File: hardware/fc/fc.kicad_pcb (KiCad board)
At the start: 6 copper layers, 35 x 35 mm, 100 parts, among them J1 USB4110-GF-A, J2 Micro_SD_Card_Det1, J3 FROM_ESC, J4 CAM, J5 CAM_CC, J6 ELRS, J7 VTX, SW1 Push, U1 TPS7A8101DRBR, U10 TPS2116DRL, U11 OPA354AIDBVR, U12 RP2354A, U2 TPS7A8101DRBR, U3 LMR51420YFDDCR, U4 USBLC6-2SC6, U5 EMIF06-MSD02N16, U6 LSM6DSK320X, U8 TS5A3159ADCK, U9 TLV7031DCKR, X1 ABM8-272-T3

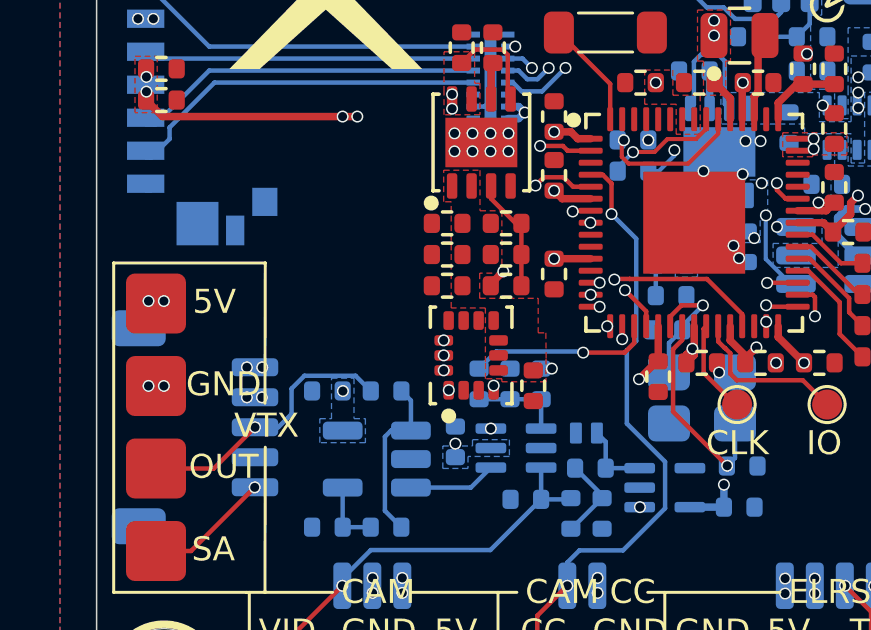
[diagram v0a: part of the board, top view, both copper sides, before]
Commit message: fc: route osd_en on l3
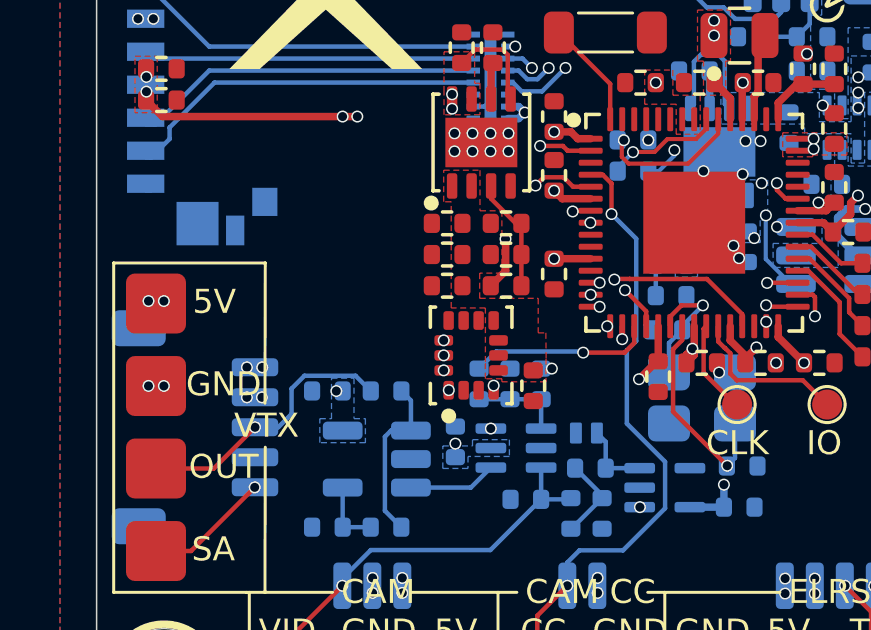
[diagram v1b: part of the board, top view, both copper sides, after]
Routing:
- net /OSD_EN: track 12.9 -> 16.6 mm
- net GND: track 6.22 -> 7.40 mm
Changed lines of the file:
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@@
 	)
 	(segment
+		(start 158.64 112.82)
+		(end 159.135 112.325)
+		(width 0.25)
+		(layer "F.Cu")
+		(net "GND")
+	)
+	(segment
 		(start 154.69 123.07)
 		(end 154.7 123.06)
@@
 	)
 	(segment
+		(start 159.135 112.325)
+		(end 159.135 111.265)
+		(width 0.25)
+		(layer "F.Cu")
+		(net "GND")
+	)
+	(segment
 		(start 167.629999 108)
 		(end 167.629999 107.998749)
@@
 	)
 	(segment
-		(start 158.640001 112.760328)
-		(end 159.056579 112.34375)
+		(start 159.135 111.265)
+		(end 159.13 111.26)
 		(width 0.25)
 		(layer "F.Cu")
@@
 	)
 	(via
-		(at 159.056579 112.34375)
-		(size 0.4)
-		(drill 0.3)
-		(layers "F.Cu" "B.Cu")
-		(net "GND")
-	)
-	(via
 		(at 162.58 126.41)
 		(size 0.4)
@@
 	)
 	(via
+		(at 159.13 111.26)
+		(size 0.4)
+		(drill 0.3)
+		(layers "F.Cu" "B.Cu")
+		(net "GND")
+	)
+	(via
 		(at 168.15 115.39)
 		(size 0.4)
@@
 	)
 	(via
-		(at 153.71 116.33)
-		(size 0.4)
-		(drill 0.3)
-		(layers "F.Cu" "B.Cu")
-		(net "V_3V3")
-	)
-	(via
 		(at 147.16 106.35)
 		(size 0.4)
@@
 	)
 	(via
+		(at 153.49 116.33)
+		(size 0.4)
+		(drill 0.3)
+		(layers "F.Cu" "B.Cu")
+		(net "V_3V3")
+	)
+	(via
 		(at 169.181044 105.090001)
 		(size 0.4)
@@
 	)
 	(segment
+		(start 153.702499 116.3275)
+		(end 153.4925 116.3275)
+		(width 0.25)
+		(layer "B.Cu")
+		(net "V_3V3")
+	)
+	(segment
 		(start 160.3175 115.582502)
 		(end 160.673812 115.582502)
@@
 	)
 	(segment
+		(start 153.4925 116.3275)
+		(end 153.49 116.33)
+		(width 0.25)
+		(layer "B.Cu")
+		(net "V_3V3")
+	)
+	(segment
 		(start 165.159999 112.110001)
 		(end 165.159999 112.22512)
@@
 	)
 	(segment
-		(start 160.130767 109.48025)
-		(end 160.130767 110.739233)
+		(start 150.965 119.54)
+		(end 150.77 119.54)
 		(width 0.15)
 		(layer "In2.Cu")
@@
 	)
 	(segment
-		(start 160.130767 110.739233)
-		(end 151.33 119.54)
+		(start 160.130767 110.789564)
+		(end 159.010331 111.91)
 		(width 0.15)
 		(layer "In2.Cu")
@@
 	)
 	(segment
-		(start 151.33 119.54)
-		(end 150.77 119.54)
+		(start 158.595 111.91)
+		(end 150.965 119.54)
+		(width 0.15)
+		(layer "In2.Cu")
+		(net "/VTX_SA")
+	)
+	(segment
+		(start 160.130767 109.48025)
+		(end 160.130767 110.789564)
+		(width 0.15)
+		(layer "In2.Cu")
+		(net "/VTX_SA")
+	)
+	(segment
+		(start 159.010331 111.91)
+		(end 158.595 111.91)
 		(width 0.15)
 		(layer "In2.Cu")
@@
 	)
 	(segment
-		(start 159.7 116.52)
-		(end 159.7 114.23)
+		(start 156.66 116.33)
+		(end 157.91 117.58)
 		(width 0.15)
-		(layer "In3.Cu")
+		(layer "In2.Cu")
 		(net "/OSD_EN")
 	)
 	(segment
-		(start 159.7 114.23)
-		(end 161.58625 112.34375)
+		(start 162.759015 112.613888)
+		(end 162.465127 112.32)
 		(width 0.15)
-		(layer "In3.Cu")
+		(layer "In2.Cu")
 		(net "/OSD_EN")
 	)
 	(segment
-		(start 158.64 117.58)
-		(end 159.7 116.52)
+		(start 158.79 112.32)
+		(end 156.66 114.45)
 		(width 0.15)
-		(layer "In3.Cu")
+		(layer "In2.Cu")
 		(net "/OSD_EN")
 	)
 	(segment
-		(start 161.58625 112.34375)
-		(end 162.488877 112.34375)
+		(start 162.465127 112.32)
+		(end 158.79 112.32)
 		(width 0.15)
-		(layer "In3.Cu")
+		(layer "In2.Cu")
 		(net "/OSD_EN")
 	)
 	(segment
-		(start 162.488877 112.34375)
-		(end 162.759015 112.613888)
+		(start 156.66 114.45)
+		(end 156.66 116.33)
 		(width 0.15)
-		(layer "In3.Cu")
+		(layer "In2.Cu")
+		(net "/OSD_EN")
+	)
+	(segment
+		(start 157.91 117.58)
+		(end 158.64 117.58)
+		(width 0.15)
+		(layer "In2.Cu")
 		(net "/OSD_EN")
 	)

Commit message: fc: clean up traces
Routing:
- net GND: track 7.40 -> 10.4 mm, vias 46 -> 48
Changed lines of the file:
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@@
 	)
 	(gr_circle
-		(center 147.749749 95.35)
-		(end 149.499749 95.35)
+		(center 147.749748 95.35)
+		(end 146.249748 95.35)
 		(stroke
-			(width 0.25)
-			(type dash)
+			(width 1)
+			(type solid)
 		)
 		(fill no)
@@
 	)
 	(gr_circle
-		(center 147.75 125.85)
-		(end 149.5 125.85)
+		(center 147.749748 125.85)
+		(end 146.249748 125.85)
 		(stroke
-			(width 0.25)
-			(type dash)
+			(width 1)
+			(type solid)
 		)
 		(fill no)
@@
 	)
 	(gr_circle
-		(center 178.25 95.35)
-		(end 180 95.35)
+		(center 178.249999 95.35)
+		(end 176.749999 95.35)
 		(stroke
-			(width 0.25)
-			(type dash)
+			(width 1)
+			(type solid)
 		)
 		(fill no)
@@
 	)
 	(gr_circle
-		(center 178.25 125.85)
-		(end 180 125.85)
+		(center 178.249999 125.85)
+		(end 176.749999 125.85)
 		(stroke
-			(width 0.25)
-			(type dash)
+			(width 1)
+			(type solid)
 		)
 		(fill no)
@@
 	)
 	(gr_circle
-		(center 147.749749 95.35)
-		(end 149.249749 95.35)
+		(center 147.749748 95.35)
+		(end 145.999748 95.35)
 		(stroke
-			(width 1)
-			(type solid)
+			(width 0.25)
+			(type dash)
 		)
 		(fill no)
@@
 	)
 	(gr_circle
-		(center 147.749749 125.85)
-		(end 149.249749 125.85)
+		(center 147.749748 125.85)
+		(end 145.999748 125.85)
 		(stroke
-			(width 1)
-			(type solid)
+			(width 0.25)
+			(type dash)
 		)
 		(fill no)
@@
 	)
 	(gr_circle
-		(center 178.25 95.35)
-		(end 179.75 95.35)
+		(center 178.249748 125.85)
+		(end 176.499748 125.85)
 		(stroke
-			(width 1)
-			(type solid)
+			(width 0.25)
+			(type dash)
 		)
 		(fill no)
@@
 	)
 	(gr_circle
-		(center 178.25 125.85)
-		(end 179.75 125.85)
+		(center 178.249999 95.35)
+		(end 176.499999 95.35)
 		(stroke
-			(width 1)
-			(type solid)
+			(width 0.25)
+			(type dash)
 		)
 		(fill no)
@@
 	)
 	(via
+		(at 158.623561 107.31875)
+		(size 0.4)
+		(drill 0.3)
+		(layers "F.Cu" "B.Cu")
+		(net "GND")
+	)
+	(via
 		(at 154.7 122.56)
 		(size 0.4)
@@
 	)
 	(via
+		(at 158.630166 104.319834)
+		(size 0.4)
+		(drill 0.3)
+		(layers "F.Cu" "B.Cu")
+		(net "GND")
+	)
+	(via
 		(at 167.631249 107.997499)
 		(size 0.4)
@@
 	)
 	(segment
+		(start 158.63 105.8475)
+		(end 158.63 107.312311)
+		(width 0.25)
+		(layer "B.Cu")
+		(net "GND")
+	)
+	(segment
+		(start 158.63 104.32)
+		(end 158.630166 104.319834)
+		(width 0.25)
+		(layer "B.Cu")
+		(net "GND")
+	)
+	(segment
+		(start 158.63 105.8475)
+		(end 158.63 104.32)
+		(width 0.25)
+		(layer "B.Cu")
+		(net "GND")
+	)
+	(segment
 		(start 171.12 110.26)
 		(end 170.490514 110.26)
@@
 	)
 	(segment
+		(start 158.63 107.312311)
+		(end 158.623561 107.31875)
+		(width 0.25)
+		(layer "B.Cu")
+		(net "GND")
+	)
+	(segment
 		(start 170.2 110.550514)
 		(end 170.2 111.169486)
@@
 	)
 	(segment
-		(start 158.774669 97.985)
+		(start 158.745 97.985)
 		(end 163.525 97.985)
 		(width 0.15)
@@
 	)
 	(segment
-		(start 158.545 98.214669)
-		(end 158.774669 97.985)
+		(start 160.284605 106.504605)
+		(end 158.24 104.46)
 		(width 0.15)
 		(layer "In2.Cu")
@@
 	)
 	(segment
-		(start 160.284605 106.504605)
-		(end 158.545 104.765)
+		(start 158.24 104.46)
+		(end 158.24 98.49)
 		(width 0.15)
 		(layer "In2.Cu")
@@
 	)
 	(segment
-		(start 163.525 97.985)
-		(end 163.91 98.37)
+		(start 160.284605 108.160001)
+		(end 160.284605 106.504605)
 		(width 0.15)
 		(layer "In2.Cu")
@@
 	)
 	(segment
-		(start 158.545 104.765)
-		(end 158.545 98.214669)
+		(start 163.525 97.985)
+		(end 163.91 98.37)
 		(width 0.15)
 		(layer "In2.Cu")
@@
 	)
 	(segment
-		(start 160.284605 108.160001)
-		(end 160.284605 106.504605)
+		(start 158.24 98.49)
+		(end 158.745 97.985)
 		(width 0.15)
 		(layer "In2.Cu")
@@
 	)
 	(segment
-		(start 163.487571 114.66276)
-		(end 163.175331 114.975)
+		(start 164.45 120.39)
+		(end 163.2 121.64)
 		(width 0.15)
 		(layer "B.Cu")
@@
 	)
 	(segment
-		(start 163.487571 111.252018)
-		(end 163.487571 114.66276)
+		(start 164.45 118.75)
+		(end 164.45 120.39)
 		(width 0.15)
 		(layer "B.Cu")
@@
 	)
 	(segment
-		(start 162.664807 110.429254)
-		(end 163.487571 111.252018)
+		(start 161.19 122.045001)
+		(end 161.19 122.82)
 		(width 0.15)
 		(layer "B.Cu")
@@
 	)
 	(segment
-		(start 163.175331 117.413299)
-		(end 164.45 118.687968)
+		(start 163.487571 111.252018)
+		(end 163.487571 115.087594)
 		(width 0.15)
 		(layer "B.Cu")
@@
 	)
 	(segment
-		(start 163.175331 114.975)
-		(end 163.175331 117.413299)
+		(start 163.487571 115.087594)
+		(end 163.175331 115.399834)
 		(width 0.15)
 		(layer "B.Cu")
@@
 	)
 	(segment
-		(start 164.45 118.687968)
-		(end 164.45 120.238656)
+		(start 163.2 121.64)
+		(end 161.595001 121.64)
 		(width 0.15)
 		(layer "B.Cu")
@@
 	)
 	(segment
-		(start 161.19 122.045001)
-		(end 161.19 122.82)
+		(start 163.175331 115.399834)
+		(end 163.175331 117.475331)
 		(width 0.15)
 		(layer "B.Cu")
@@
 	)
 	(segment
-		(start 163.048656 121.64)
-		(end 161.595001 121.64)
+		(start 162.664807 110.429254)
+		(end 163.487571 111.252018)
 		(width 0.15)
 		(layer "B.Cu")
@@
 	)
 	(segment
-		(start 164.45 120.238656)
-		(end 163.048656 121.64)
+		(start 163.175331 117.475331)
+		(end 164.45 118.75)
 		(width 0.15)
 		(layer "B.Cu")
@@
 	)
 	(segment
-		(start 163.205001 119.795001)
-		(end 163.61 120.2)
+		(start 163.205001 115.384999)
+		(end 163.205001 119.795001)
 		(width 0.15)
 		(layer "In2.Cu")
@@
 	)
 	(segment
-		(start 163.49 115.494138)
-		(end 163.205001 115.779137)
+		(start 163.49 113.344872)
+		(end 163.49 115.1)
 		(width 0.15)
 		(layer "In2.Cu")
@@
 	)
 	(segment
-		(start 163.205001 115.779137)
-		(end 163.205001 119.795001)
+		(start 163.205001 119.795001)
+		(end 163.61 120.2)
 		(width 0.15)
 		(layer "In2.Cu")
@@
 	)
 	(segment
-		(start 163.49 113.344872)
-		(end 163.49 115.494138)
+		(start 163.49 115.1)
+		(end 163.205001 115.384999)
 		(width 0.15)
 		(layer "In2.Cu")

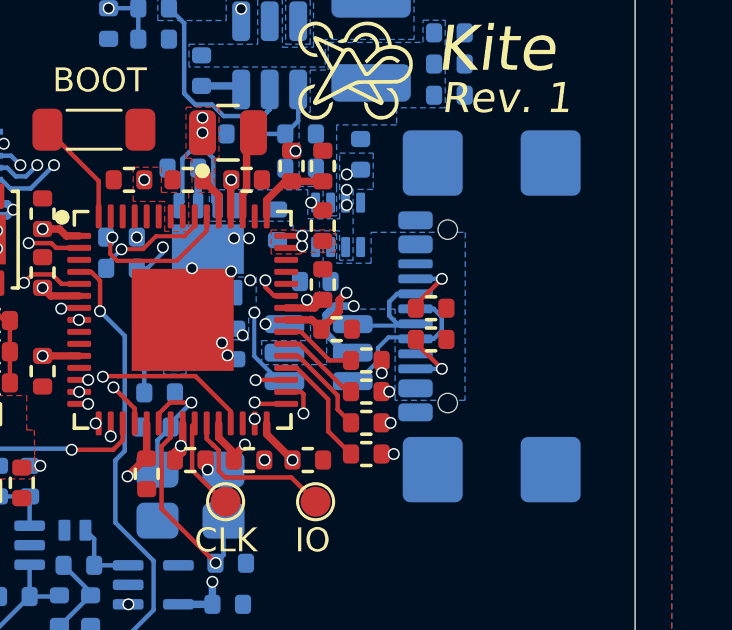
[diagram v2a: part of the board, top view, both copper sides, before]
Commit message: fc: add LEDs
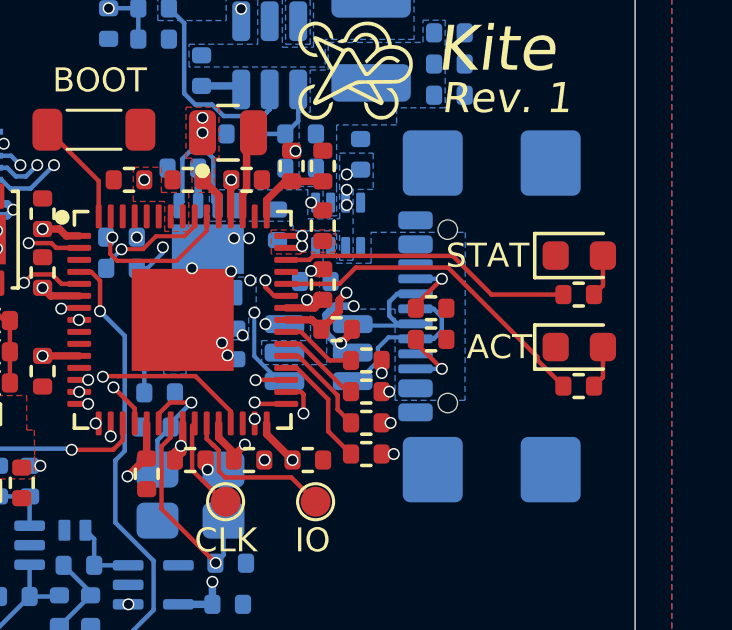
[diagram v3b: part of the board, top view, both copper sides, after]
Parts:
- added D2: Green, LED_SMD:LED_0603_1608Metric, F.Cu at (178.6, 108.6)
- added D3: Green, LED_SMD:LED_0603_1608Metric, F.Cu at (178.6, 111.6)
- added R26: 1k, Stratus:R_0402, F.Cu at (178.6, 109.9)
- added R27: 1k, Stratus:R_0402, F.Cu at (178.6, 112.9)
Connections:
- U12 pad 42: unconnected-(U12-GPIO28/ADC2-Pad42) -> /LED1
- U12 pad 43: unconnected-(U12-GPIO29/ADC3-Pad43) -> /LED0
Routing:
- net /LED1: track 0.00 -> 11.2 mm
- net /LED0: track 0.00 -> 9.83 mm
- net Net-(D3-A): track 0.00 -> 1.42 mm
- net Net-(D2-A): track 0.00 -> 1.42 mm
- net GND: track 10.4 -> 11.4 mm, vias 48 -> 50
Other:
- board text added: "ACT"
- board text added: "STAT"

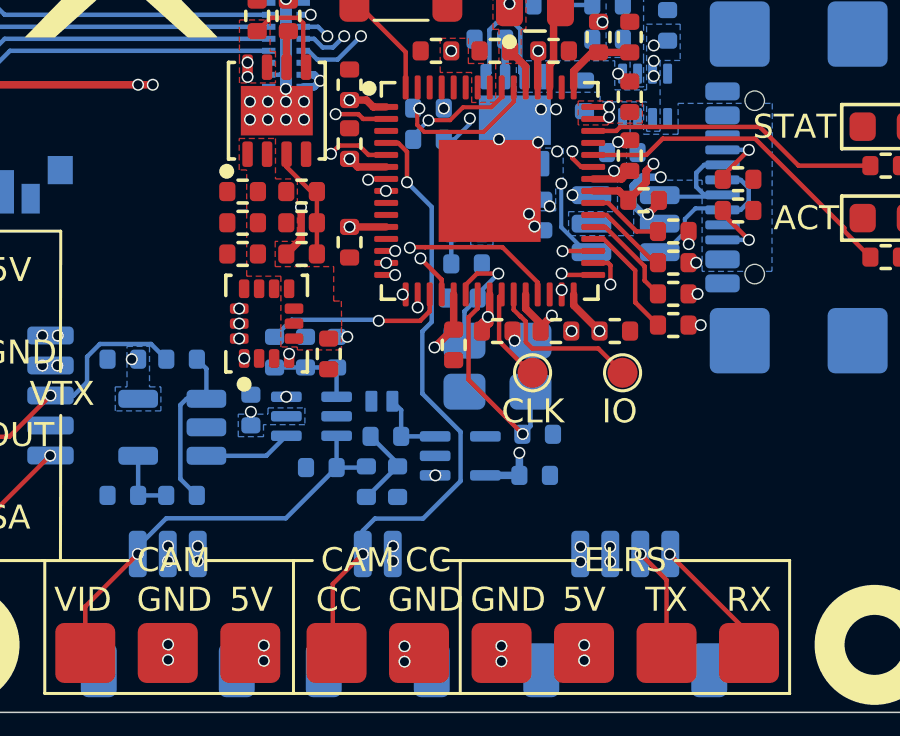
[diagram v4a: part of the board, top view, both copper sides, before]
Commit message: fc: add rbleed, swap comparator, clamp video to vref
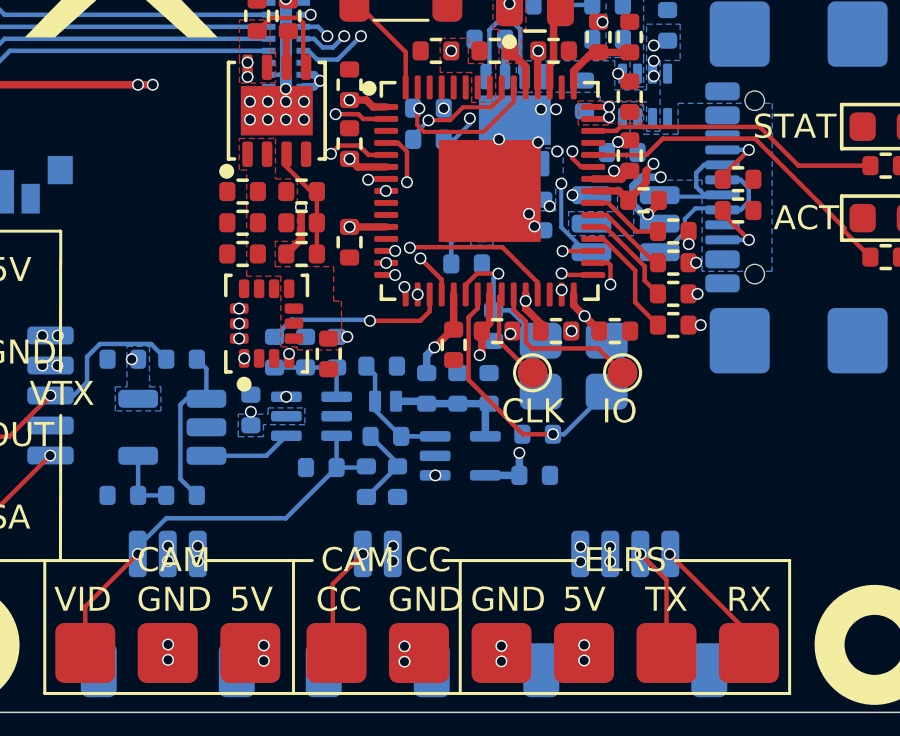
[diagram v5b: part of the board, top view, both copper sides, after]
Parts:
- added C48: 0.1uF, Stratus:C_0402, B.Cu at (165.4, 117.3)
- added R28: 100k, Stratus:R_0402, B.Cu at (161.8, 116.6)
- added R29: 10k, Stratus:R_0402, B.Cu at (163.3, 117.3)
- added R30: 1.5k, Stratus:R_0402, B.Cu at (164.4, 117.3)
- R12: value 1.4k -> 3.24k
- U9: value TLV7031DCKR -> LMV7219M7X; footprint Stratus:TLV7031DCKR -> Stratus:LMV7219M7X_NOPB
- moved X1 2.54 mm to (168.2, 116.6)
- moved C32 1.39 mm to (165.6, 115.2), turned to -90 degrees
- moved D1 0.12 mm to (161.9, 117.7), turned to 0 degrees
- turned C33 to 180 degrees
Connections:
- D1 pad 2: GND -> /OSD/V_REF
- U12 pad 41: unconnected-(U12-GPIO27/ADC1-Pad41) -> /LED1
- U12 pad 42: /LED1 -> unconnected-(U12-GPIO28/ADC2-Pad42)
- U9 pad 4: GND -> /OSD/V_REF
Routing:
- net /OSD/V_REF: track 0.00 -> 4.27 mm
- net /CC: track 21.2 -> 23.3 mm
- net Net-(U12-XOUT): track 7.06 -> 8.92 mm
- net V_1V1: track 26.9 -> 28.6 mm
- net Net-(D1-K): track 2.42 -> 3.95 mm
- net V_3V3: track 24.5 -> 25.9 mm
- net /OSD_W: track 6.12 -> 6.92 mm
- net Net-(U12-XIN): track 4.27 -> 4.84 mm

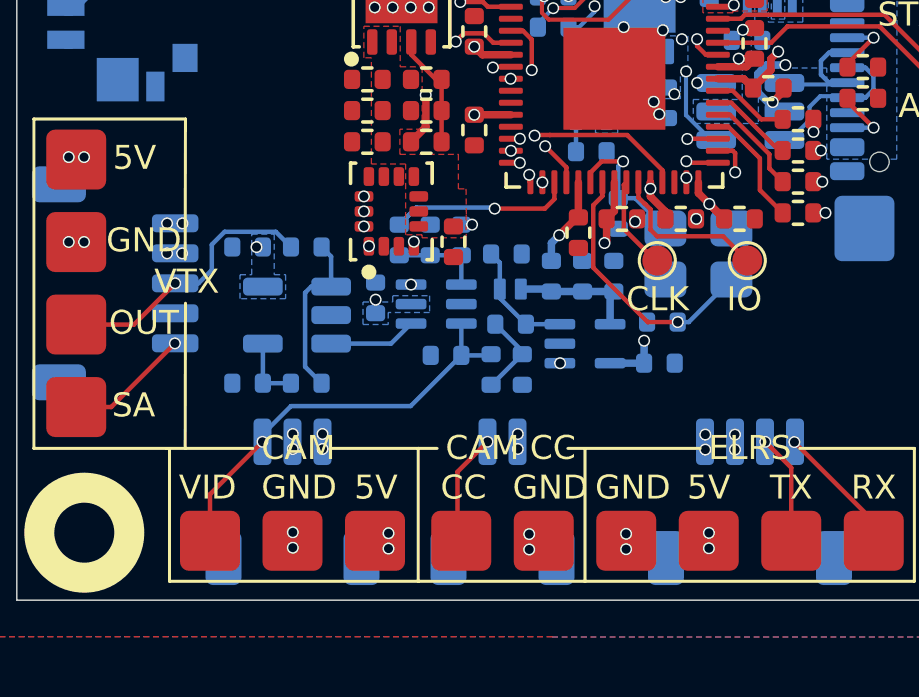
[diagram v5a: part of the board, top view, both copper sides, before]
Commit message: fc: move DC restoration/clamp to shared path
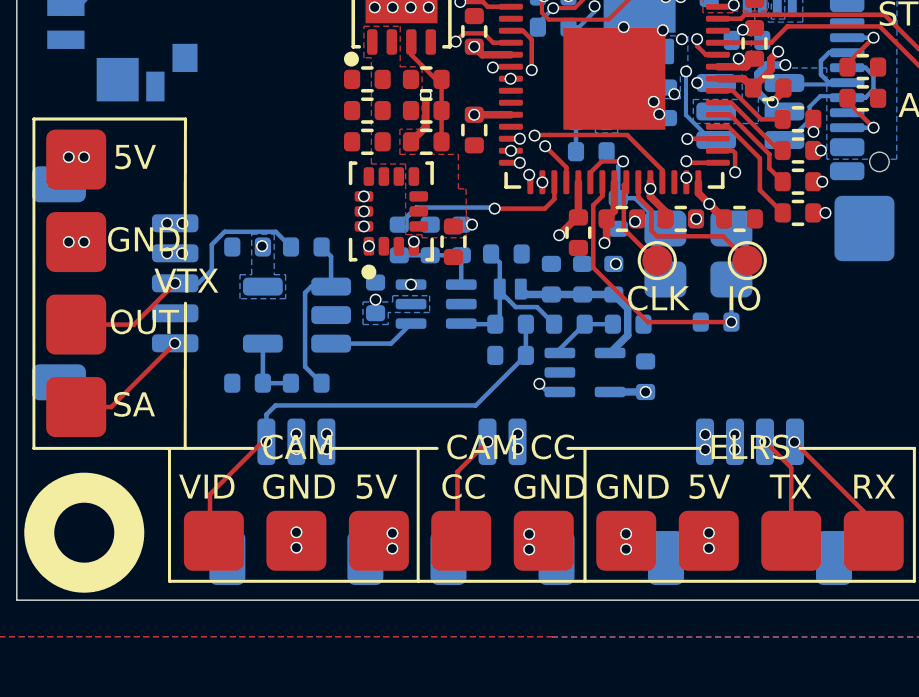
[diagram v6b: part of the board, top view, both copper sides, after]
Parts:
- C32, C33: value 15p -> 15pF
- R10: value 10k -> 2k
- R11: value 24.9k -> 3.09k
- R12: value 3.24k -> 649R
- R30: value 1.5k -> 1.2k
- moved C26 3.84 mm to (165.9, 118.9), turned to 0 degrees
- moved R16 3.02 mm to (163.9, 118.9), turned to 0 degrees
- moved R9 2.15 mm to (162.0, 119.9)
- moved C48 2.08 mm to (163.3, 117.4)
- moved R29 2.08 mm to (165.4, 117.4)
- moved C33 1.79 mm to (168.8, 118.8)
- moved U9 0.96 mm to (164.4, 120.5)
- moved C28 0.64 mm to (166.5, 120.7), turned to 90 degrees
- moved J4 0.13 mm to (154.8, 124.8)
- moved R30 0.10 mm to (164.4, 117.4)
- turned C27 to 0 degrees
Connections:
- C26 pad 1: Net-(C26-Pad1) -> Net-(U9-+)
- C27 pad 2: Net-(C26-Pad1) -> /OSD/VIDEO_IN
- R16 pad 1: /OSD/VIDEO_IN -> Net-(D1-K)
- R16 pad 2: Net-(C26-Pad1) -> Net-(U9-+)
- U8 pad 3: /OSD/VIDEO_IN -> Net-(D1-K)
- U9 pad 3: Net-(D1-K) -> Net-(U9-+)
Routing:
- net Net-(C26-Pad1): track 2.84 -> 0.00 mm
- net Net-(U9-+): track 0.00 -> 2.24 mm
- net Net-(D1-K): track 3.95 -> 6.00 mm
- net V_3V3: track 25.9 -> 24.1 mm, vias 22 -> 23
- net /OSD/VIDEO_IN: track 14.1 -> 15.6 mm
- net /OSD_SYNC: track 9.18 -> 10.6 mm
- net /OSD/V_REF: track 4.27 -> 5.67 mm
- net Net-(U12-XOUT): track 8.92 -> 9.75 mm
